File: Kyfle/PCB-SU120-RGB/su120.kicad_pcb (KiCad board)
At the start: 2 copper layers, 98.8 x 98 mm, 429 parts, among them J1 MJ-4PP-9, J2 Conn_01x03, J3 Conn_01x08, J4 Conn_01x08, J5 Conn_01x03, J6 MJ-4PP-9, J7 Conn_02x05_Odd_Even, J8 Conn_02x05_Odd_Even, SW1 SW_PUSH_LED, SW10 SW_PUSH_LED, SW11 SW_PUSH_LED, SW12 SW_PUSH_LED, SW13 SW_PUSH_LED, SW14 SW_PUSH_LED, SW15 SW_PUSH_LED, SW16 SW_PUSH_LED, SW17 SW_PUSH_LED, SW18 SW_PUSH_LED, SW2 SW_PUSH_LED, SW20 Rotary_Encoder_Switch, SW21 Rotary_Encoder_Switch, SW22 SW_Push, SW3 SW_PUSH_LED, SW4 SW_PUSH_LED, SW5 SW_PUSH_LED, SW6 SW_PUSH_LED, SW7 SW_PUSH_LED, SW8 SW_PUSH_LED, SW9 SW_PUSH_LED, U1 ProMicro

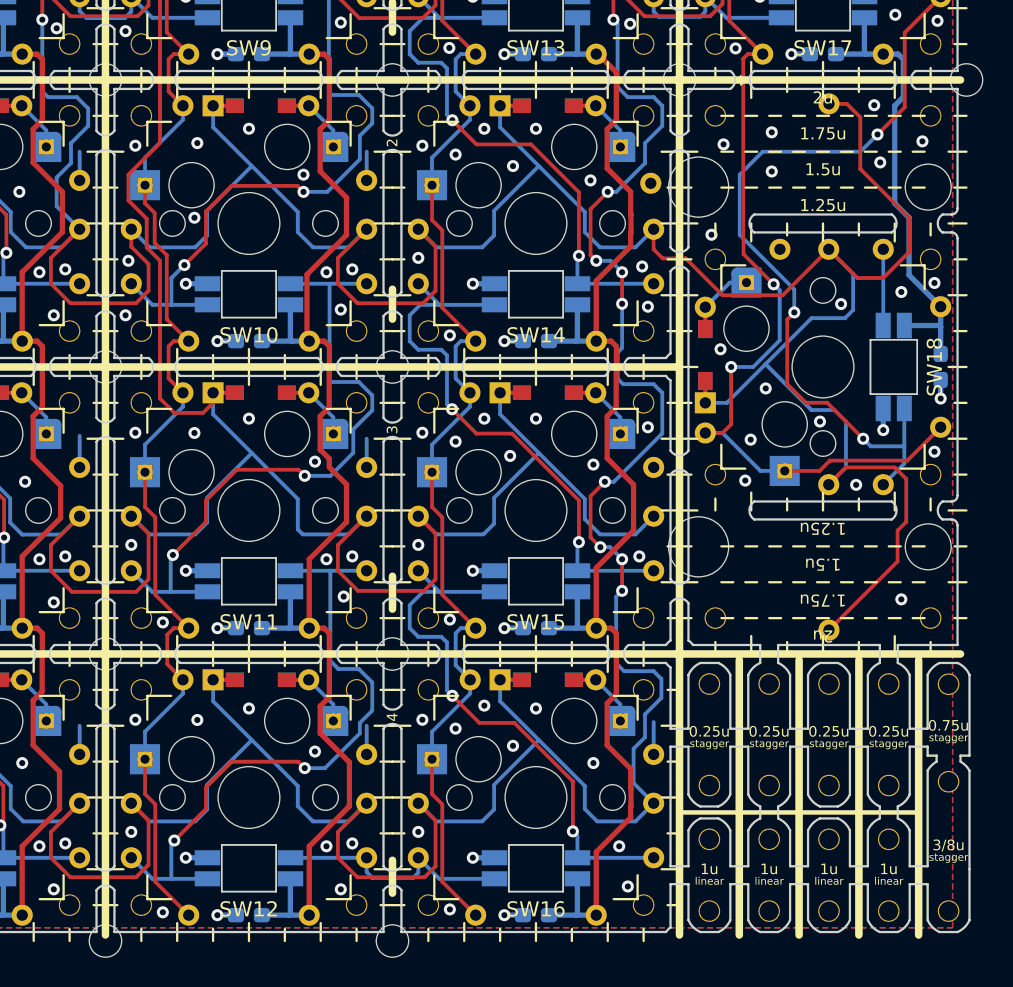
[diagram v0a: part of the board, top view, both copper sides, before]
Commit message: Adding 4 RGB bit boards to the PCB
Replacing some of the spacers.
Based on SK6812 Mini-E.
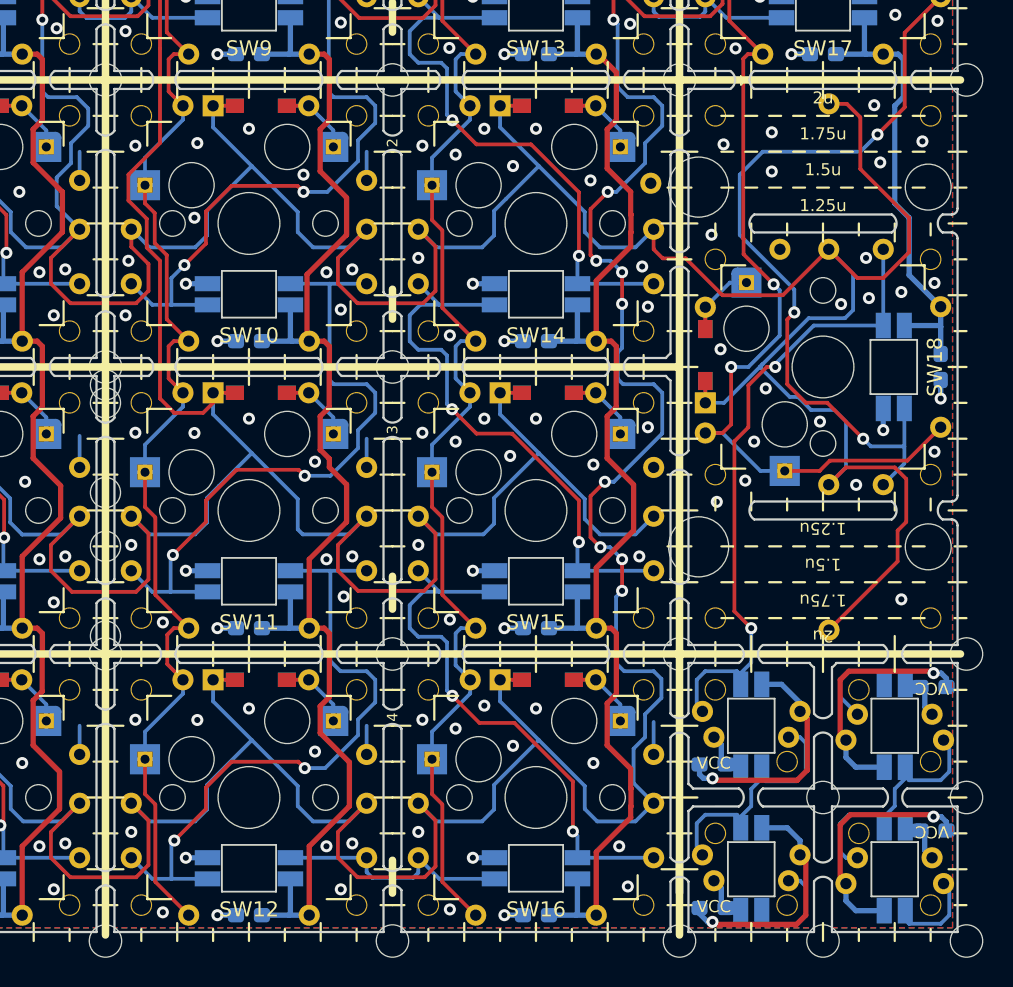
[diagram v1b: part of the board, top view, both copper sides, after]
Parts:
- removed the ? at (124.2, 150.4)
- removed the ? at (124.2, 142.1)
- removed the ? at (120.3, 142.1)
- removed the ? at (120.3, 135.3)
- removed the ? at (124.2, 145.7)
- removed the ? at (124.2, 135.3)
- removed the ? at (120.3, 150.4)
- removed the ? at (120.3, 145.7)
- removed the ? at (128.2, 142.1)
- removed the ? at (128.2, 145.7)
- removed the ? at (128.2, 135.3)
- removed the ? at (128.2, 150.4)
- removed the ? at (132.2, 142.1)
- removed the ? at (132.2, 145.7)
- removed the ? at (132.2, 135.3)
- removed the ? at (132.2, 150.4)
- removed the ? at (136.1, 135.4)
- removed the ? at (136.1, 150.4)
- removed the ? at (136.1, 141.8)
- added ?: , #footprint:M2_Hole, F.Cu at (80.2, 126.2)
- added ?: , #footprint:M2_Hole, F.Cu at (137.3, 142.9)
- added ?: , #footprint:M2_Hole, F.Cu at (137.3, 133.3)
- added ?: , #footprint:M1.4_tapping_Hole_rev2, F.Cu at (130.2, 135.7)
- added ?: , #footprint:M1.4_tapping_Hole_rev2, F.Cu at (125.4, 140.5)
- added ?: , #footprint:M1.4_tapping_Hole_rev2, F.Cu at (125.4, 150.0)
- added ?: , #footprint:M1.4_tapping_Hole_rev2, F.Cu at (130.2, 145.3)
- added ?: , #footprint:M1.4_tapping_Hole_rev2, F.Cu at (134.9, 140.5)
- added ?: , #footprint:M1.4_tapping_Hole_rev2, F.Cu at (120.7, 145.3)
- added ?: , #footprint:M2_Hole, F.Cu at (118.3, 133.3)
- added ?: , #footprint:M2_Hole, F.Cu at (118.3, 152.4)
- added ?: , #footprint:M2_Hole, F.Cu at (80.2, 116.7)
- added ?: , #footprint:M1.4_tapping_Hole_rev2, F.Cu at (134.9, 150.0)
- added ?: , #footprint:M1.4_tapping_Hole_rev2, F.Cu at (120.7, 135.7)
- added ?: , #footprint:M2_Hole, F.Cu at (80.2, 115.5)
- added ?: , #footprint:M2_Hole, F.Cu at (80.2, 122.6)
- added ?: , #footprint:M2_Hole, F.Cu at (80.2, 132.2)
- added ?: , #footprint:CherryMX_MidHeight_Choc_Silk, F.Cu at (127.8, 142.9)
- added ?: , #footprint:M2_Hole, F.Cu at (127.8, 142.9)
- added ?: , #footprint:M2_Hole, F.Cu at (137.3, 152.4)
- added ?: , #footprint:M2_Hole, F.Cu at (127.8, 152.4)
- added C19: 100n, Capacitor_SMD:C_0603_1608Metric_Pad1.08x0.95mm_HandSolder, B.Cu at (120.5, 140.7)
- added C20: 100n, Capacitor_SMD:C_0603_1608Metric_Pad1.08x0.95mm_HandSolder, B.Cu at (120.5, 150.2)
- added C21: 100n, Capacitor_SMD:C_0603_1608Metric_Pad1.08x0.95mm_HandSolder, B.Cu at (135.1, 145.1)
- added C22: 100n, Capacitor_SMD:C_0603_1608Metric_Pad1.08x0.95mm_HandSolder, B.Cu at (135.1, 135.5)
- added H152: MountingHole_Pad, #footprint:1pin_conn, F.Cu at (120.6, 138.9)
- added H153: MountingHole_Pad, #footprint:1pin_conn, F.Cu at (125.5, 138.9)
- added H154: MountingHole_Pad, #footprint:1pin_conn, F.Cu at (119.8, 137.2)
- added H155: MountingHole_Pad, #footprint:1pin_conn, F.Cu at (126.3, 137.2)
- added H156: MountingHole_Pad, #footprint:1pin_conn, F.Cu at (120.6, 148.4)
- added H157: MountingHole_Pad, #footprint:1pin_conn, F.Cu at (125.5, 148.4)
- added H158: MountingHole_Pad, #footprint:1pin_conn, F.Cu at (119.8, 146.7)
- added H159: MountingHole_Pad, #footprint:1pin_conn, F.Cu at (126.3, 146.7)
- added H160: MountingHole_Pad, #footprint:1pin_conn, F.Cu at (135.0, 146.9)
- added H161: MountingHole_Pad, #footprint:1pin_conn, F.Cu at (130.1, 146.9)
- added H162: MountingHole_Pad, #footprint:1pin_conn, F.Cu at (135.8, 148.6)
- added H163: MountingHole_Pad, #footprint:1pin_conn, F.Cu at (129.3, 148.6)
- added H164: MountingHole_Pad, #footprint:1pin_conn, F.Cu at (135.0, 137.4)
- added H165: MountingHole_Pad, #footprint:1pin_conn, F.Cu at (130.1, 137.4)
- added H166: MountingHole_Pad, #footprint:1pin_conn, F.Cu at (135.8, 139.1)
- added H167: MountingHole_Pad, #footprint:1pin_conn, F.Cu at (129.3, 139.1)
- added SW19: LED_SK6812_Mini_E, #footprint:SK6812_Mini_E, B.Cu at (123.0, 147.6)
- added SW23: LED_SK6812_Mini_E, #footprint:SK6812_Mini_E, B.Cu at (132.6, 147.6)
- added SW24: LED_SK6812_Mini_E, #footprint:SK6812_Mini_E, B.Cu at (132.6, 138.1)
- added SW?1: LED_SK6812_Mini_E, #footprint:SK6812_Mini_E, B.Cu at (123.0, 138.1)
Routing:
- net GND: track 358.9 -> 423.1 mm, vias 250 -> 256
- net Net-(H154-Pad1): track 5.06 -> 42.9 mm, vias 0 -> 2
- net Net-(H153-Pad1): track 0.00 -> 17.9 mm
- net Net-(H161-Pad1): track 0.00 -> 17.8 mm
- net Net-(H157-Pad1): track 0.00 -> 13.4 mm
- net VCC: track 452.5 -> 465.4 mm
- net Net-(H165-Pad1): track 0.00 -> 6.64 mm
- net Y2: track 312.8 -> 313.4 mm
- net (no net): vias 0 -> 1
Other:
- board size 98.8 x 98 mm -> 98 x 98 mm
- board text removed: "0.75u"

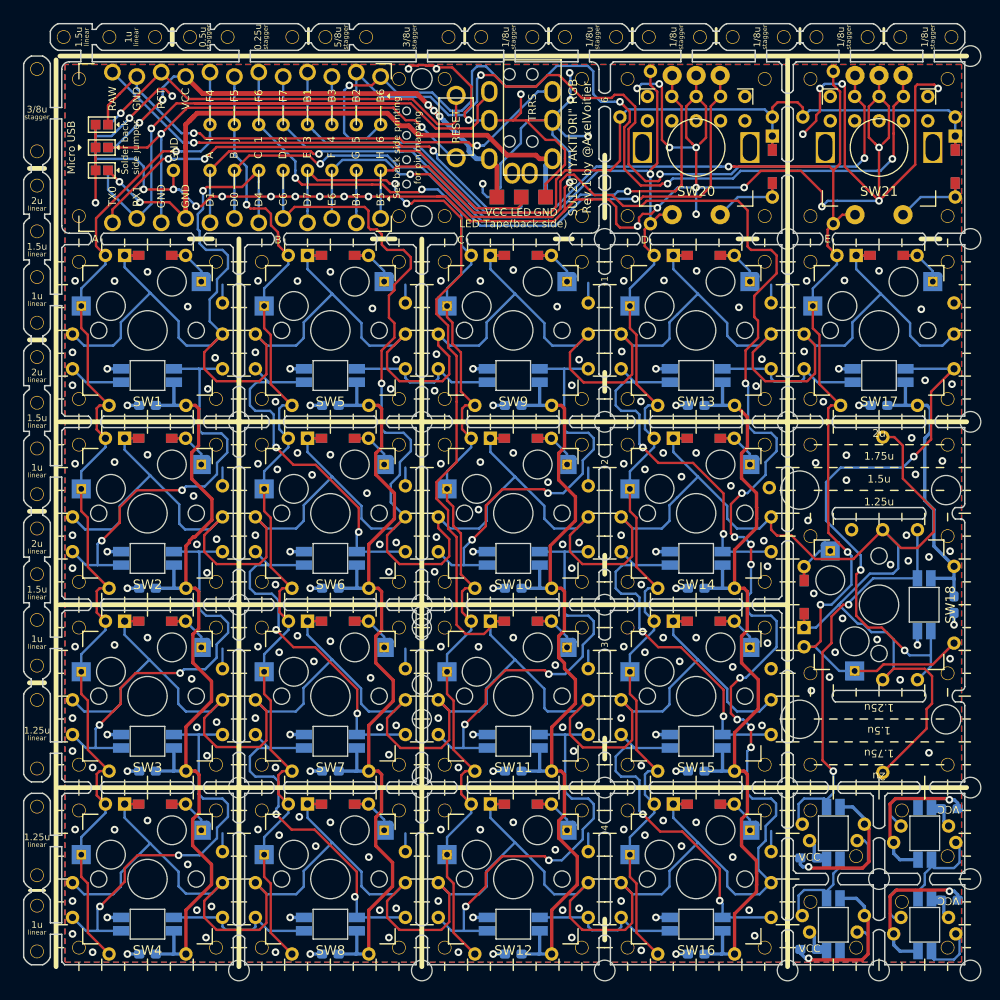
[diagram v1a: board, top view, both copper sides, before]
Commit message: Experimentation with different fastening solutions. Not great.
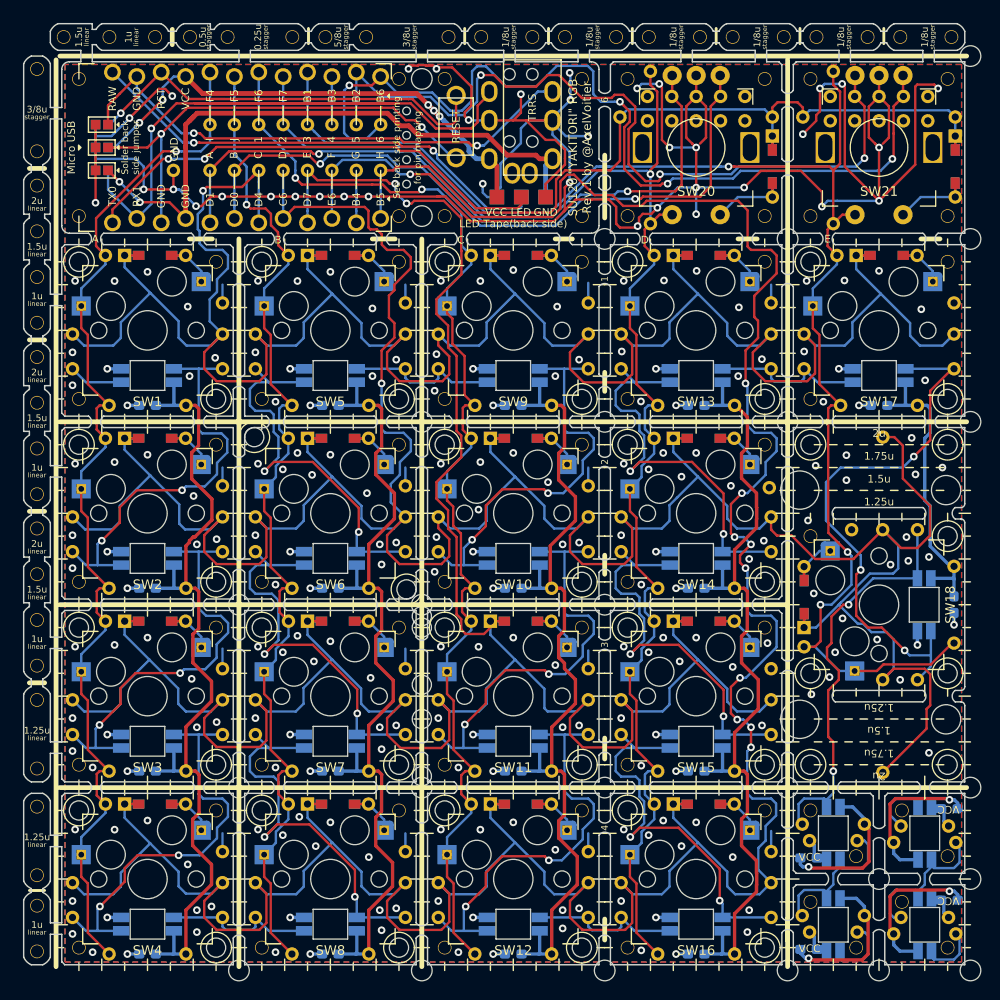
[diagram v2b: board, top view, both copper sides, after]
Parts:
- removed the ? at (115.9, 111.9)
- removed the ? at (96.8, 111.9)
- removed the ? at (77.8, 111.9)
- removed the ? at (58.7, 111.9)
- removed the ? at (44.5, 116.7)
- removed the ? at (63.5, 116.7)
- removed the ? at (82.5, 116.7)
- removed the ? at (101.6, 116.7)
- removed the ? at (63.5, 135.7)
- removed the ? at (77.8, 150.0)
- removed the ? at (115.9, 131.0)
- removed the ? at (96.8, 131.0)
- removed the ? at (77.8, 131.0)
- removed the ? at (58.7, 131.0)
- removed the ? at (120.7, 131.0)
- removed the ? at (120.7, 121.4)
- removed the ? at (120.7, 97.6)
- removed the ? at (101.6, 135.7)
- removed the ? at (82.5, 135.7)
- removed the ? at (96.8, 150.0)
- removed the ? at (115.9, 150.0)
- removed the ? at (134.9, 97.6)
- removed the ? at (134.9, 107.2)
- removed the ? at (134.9, 121.4)
- removed the ? at (134.9, 131.0)
- removed the ? at (61.1, 95.3)
- removed the ? at (44.5, 78.6)
- removed the ? at (63.5, 78.6)
- removed the ? at (82.5, 78.6)
- removed the ? at (101.6, 78.6)
- removed the ? at (120.7, 78.6)
- removed the ? at (134.9, 92.9)
- removed the ? at (115.9, 92.9)
- removed the ? at (96.8, 92.9)
- removed the ? at (77.8, 92.9)
- removed the ? at (58.7, 92.9)
- removed the ? at (44.5, 97.6)
- removed the ? at (63.5, 97.6)
- removed the ? at (82.5, 97.6)
- removed the ? at (101.6, 97.6)
- removed the ? at (44.5, 135.7)
- removed the ? at (58.7, 150.0)
- added Ref**: Val**, #footprint:M2_Hole_Standoff, F.Cu at (134.9, 121.4)
- added Ref**: Val**, #footprint:M2_Hole_Standoff, F.Cu at (82.5, 135.7)
- added Ref**: Val**, #footprint:M2_Hole_Standoff, F.Cu at (101.6, 135.7)
- added Ref**: Val**, #footprint:M2_Hole_Standoff, F.Cu at (101.6, 116.7)
- added Ref**: Val**, #footprint:M2_Hole_Standoff, F.Cu at (82.5, 116.7)
- added Ref**: Val**, #footprint:M2_Hole_Standoff, F.Cu at (63.5, 116.7)
- added Ref**: Val**, #footprint:M2_Hole_Standoff, F.Cu at (44.5, 116.7)
- added Ref**: Val**, #footprint:M2_Hole_Standoff, F.Cu at (44.5, 97.6)
- added Ref**: Val**, #footprint:M2_Hole_Standoff, F.Cu at (62.7, 96.8)
- added Ref**: Val**, #footprint:M2_Hole_Standoff, F.Cu at (82.5, 97.6)
- added Ref**: Val**, #footprint:M2_Hole_Standoff, F.Cu at (101.6, 97.6)
- added Ref**: Val**, #footprint:M2_Hole_Standoff, F.Cu at (134.9, 107.2)
- added Ref**: Val**, #footprint:M2_Hole_Standoff, F.Cu at (120.7, 78.6)
- added Ref**: Val**, #footprint:M2_Hole_Standoff, F.Cu at (101.6, 78.6)
- added Ref**: Val**, #footprint:M2_Hole_Standoff, F.Cu at (82.5, 78.6)
- added Ref**: Val**, #footprint:M2_Hole_Standoff, F.Cu at (63.5, 78.6)
- added Ref**: Val**, #footprint:M2_Hole_Standoff, F.Cu at (44.5, 78.6)
- added Ref**: Val**, #footprint:M2_Hole_Standoff, F.Cu at (58.7, 150.0)
- added Ref**: Val**, #footprint:M2_Hole_Standoff, F.Cu at (77.8, 150.0)
- added Ref**: Val**, #footprint:M2_Hole_Standoff, F.Cu at (96.8, 150.0)
- added Ref**: Val**, #footprint:M2_Hole_Standoff, F.Cu at (115.9, 150.0)
- added Ref**: Val**, #footprint:M2_Hole_Standoff, F.Cu at (115.9, 131.0)
- added Ref**: Val**, #footprint:M2_Hole_Standoff, F.Cu at (120.7, 121.4)
- added Ref**: Val**, #footprint:M2_Hole_Standoff, F.Cu at (96.8, 131.0)
- added Ref**: Val**, #footprint:M2_Hole_Standoff, F.Cu at (77.8, 131.0)
- added Ref**: Val**, #footprint:M2_Hole_Standoff, F.Cu at (58.7, 131.0)
- added Ref**: Val**, #footprint:M2_Hole_Standoff, F.Cu at (58.7, 111.9)
- added Ref**: Val**, #footprint:M2_Hole_Standoff, F.Cu at (78.6, 112.7)
- added Ref**: Val**, #footprint:M2_Hole_Standoff, F.Cu at (96.8, 111.9)
- added Ref**: Val**, #footprint:M2_Hole_Standoff, F.Cu at (115.9, 111.9)
- added Ref**: Val**, #footprint:M2_Hole_Standoff, F.Cu at (134.9, 92.9)
- added Ref**: Val**, #footprint:M2_Hole_Standoff, F.Cu at (115.9, 92.9)
- added Ref**: Val**, #footprint:M2_Hole_Standoff, F.Cu at (96.8, 92.9)
- added Ref**: Val**, #footprint:M2_Hole_Standoff, F.Cu at (120.7, 131.0)
- added Ref**: Val**, #footprint:M2_Hole_Standoff, F.Cu at (77.8, 92.9)
- added Ref**: Val**, #footprint:M2_Hole_Standoff, F.Cu at (58.7, 92.9)
- added Ref**: Val**, #footprint:M2_Hole_Standoff, F.Cu at (134.9, 131.0)
- added Ref**: Val**, #footprint:M2_Hole_Standoff, F.Cu at (134.9, 97.6)
- added Ref**: Val**, #footprint:M2_Hole_Standoff, F.Cu at (120.7, 97.6)
- added Ref**: Val**, #footprint:M2_Hole_Standoff, F.Cu at (44.5, 135.7)
- added Ref**: Val**, #footprint:M2_Hole_Standoff, F.Cu at (63.5, 135.7)
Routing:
- net Net-(H102-Pad1): track 37.5 -> 41.7 mm
- net Net-(H65-Pad1): track 36.9 -> 41.1 mm
- net Net-(H106-Pad1): track 36.7 -> 40.8 mm
- net Net-(H104-Pad1): track 36.9 -> 41.0 mm
- net Net-(H149-Pad1): track 37.3 -> 41.3 mm
- net Net-(H67-Pad1): track 37.1 -> 41.1 mm
- net Y4: track 319.9 -> 320.6 mm
- net Net-(H154-Pad1): track 42.9 -> 43.4 mm
- net GND: vias 256 -> 249
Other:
- outline, holes or cut-outs redrawn

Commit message: Cleaning up the mounting points tests, increasing the mounting points of remaining bits (pro micro, potentiometer, 2u key). And strenghtening the power tracks to accomodate possible "high" current when using LEDs.
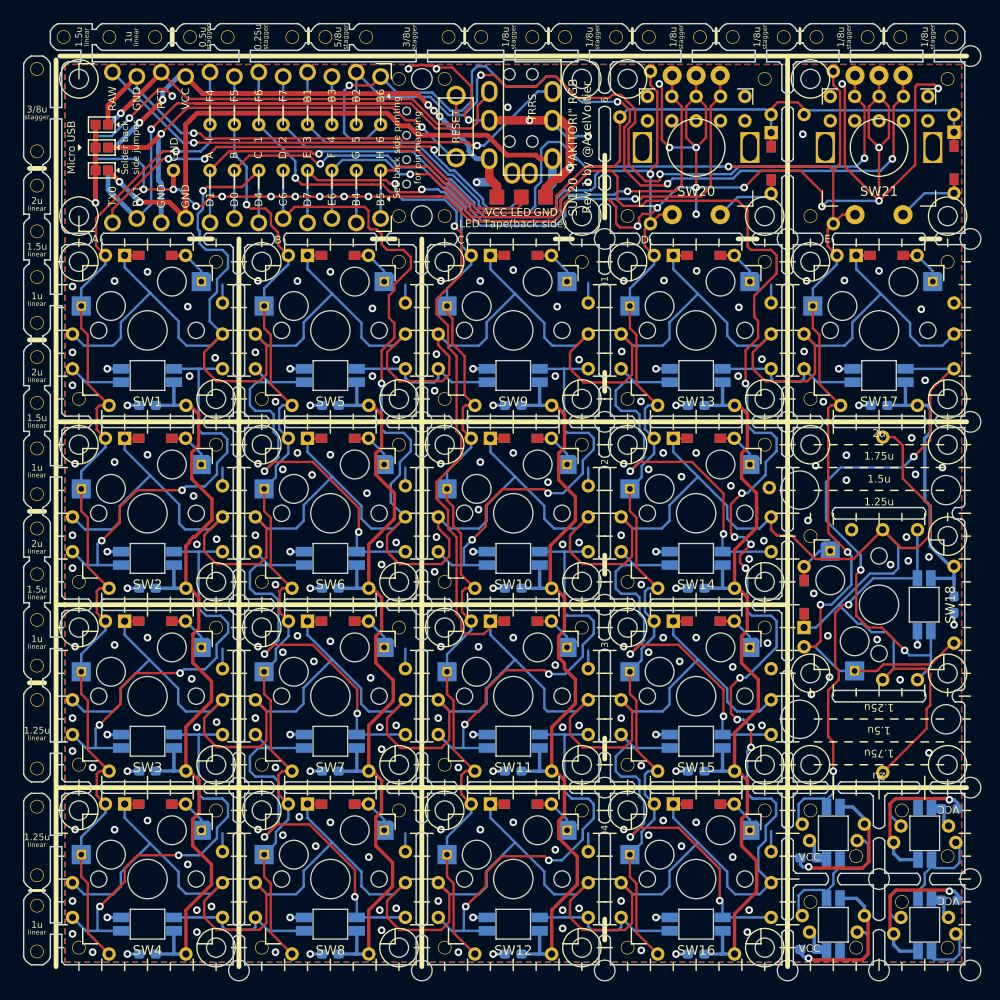
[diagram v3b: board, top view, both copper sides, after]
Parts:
- removed the ? at (80.2, 132.2)
- removed the ? at (80.2, 126.2)
- removed the ? at (80.2, 122.6)
- removed the ? at (80.2, 116.7)
- removed the ? at (80.2, 115.5)
- added ?: , #footprint:M2_Hole, F.Cu at (61.1, 95.3)
- ? (x8): footprint #footprint:M1.4_tapping_Hole_rev2 -> #footprint:M2_Hole_Standoff
- moved Ref** 1.11 mm to (63.5, 97.6)
- moved Ref** 1.11 mm to (77.8, 111.9)
- moved D19 0.42 mm to (135.6, 65.5)
- moved D18 0.37 mm to (116.6, 65.5)
- moved H139 0.28 mm to (120.0, 63.2)
- moved H138 0.28 mm to (116.6, 63.2)
- moved H140 0.28 mm to (135.6, 63.2)
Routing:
- net GND: track 423.1 -> 391.0 mm, vias 249 -> 246
- net X5: track 161.5 -> 167.0 mm
- net VCC: track 465.6 -> 461.9 mm
- net X4: track 169.2 -> 171.8 mm
- net X2: track 117.3 -> 119.5 mm
- net X8: track 95.2 -> 93.0 mm
- net Y6: track 88.6 -> 86.6 mm
- net dummyVCC: track 57.0 -> 55.3 mm
- net X9: track 75.2 -> 76.4 mm
- net X10: track 73.8 -> 74.8 mm
- net Net-(H154-Pad1): track 43.4 -> 42.7 mm
- net Y4: track 320.6 -> 321.3 mm
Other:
- outline, holes or cut-outs redrawn
